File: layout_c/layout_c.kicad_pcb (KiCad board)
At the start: 2 copper layers, 84.9 x 53.1 mm, 74 parts, among them J1 platform UART, J10 Conn_01x08, J11 TSM-113-01-L-DH-A-P-TR, J12 Conn_01x04, J2 USB_C_Sensors, J3 CSI2 Camera, J4 Lidar, J5 MSD-4-A, J6 Power, J7 Radar UART, J8 Conn_01x11, J9 USB_C_Radar, Q1 TSM500P02CX_RFG, SW1 RST, U1 MLX90614ESF-BAA-000-TU, U2 USBLC6-2SC6, U3 BNO085, U4 USBLC6-2SC6, U5 ESP32-P4_MODULE, U9 DRV8434PWP

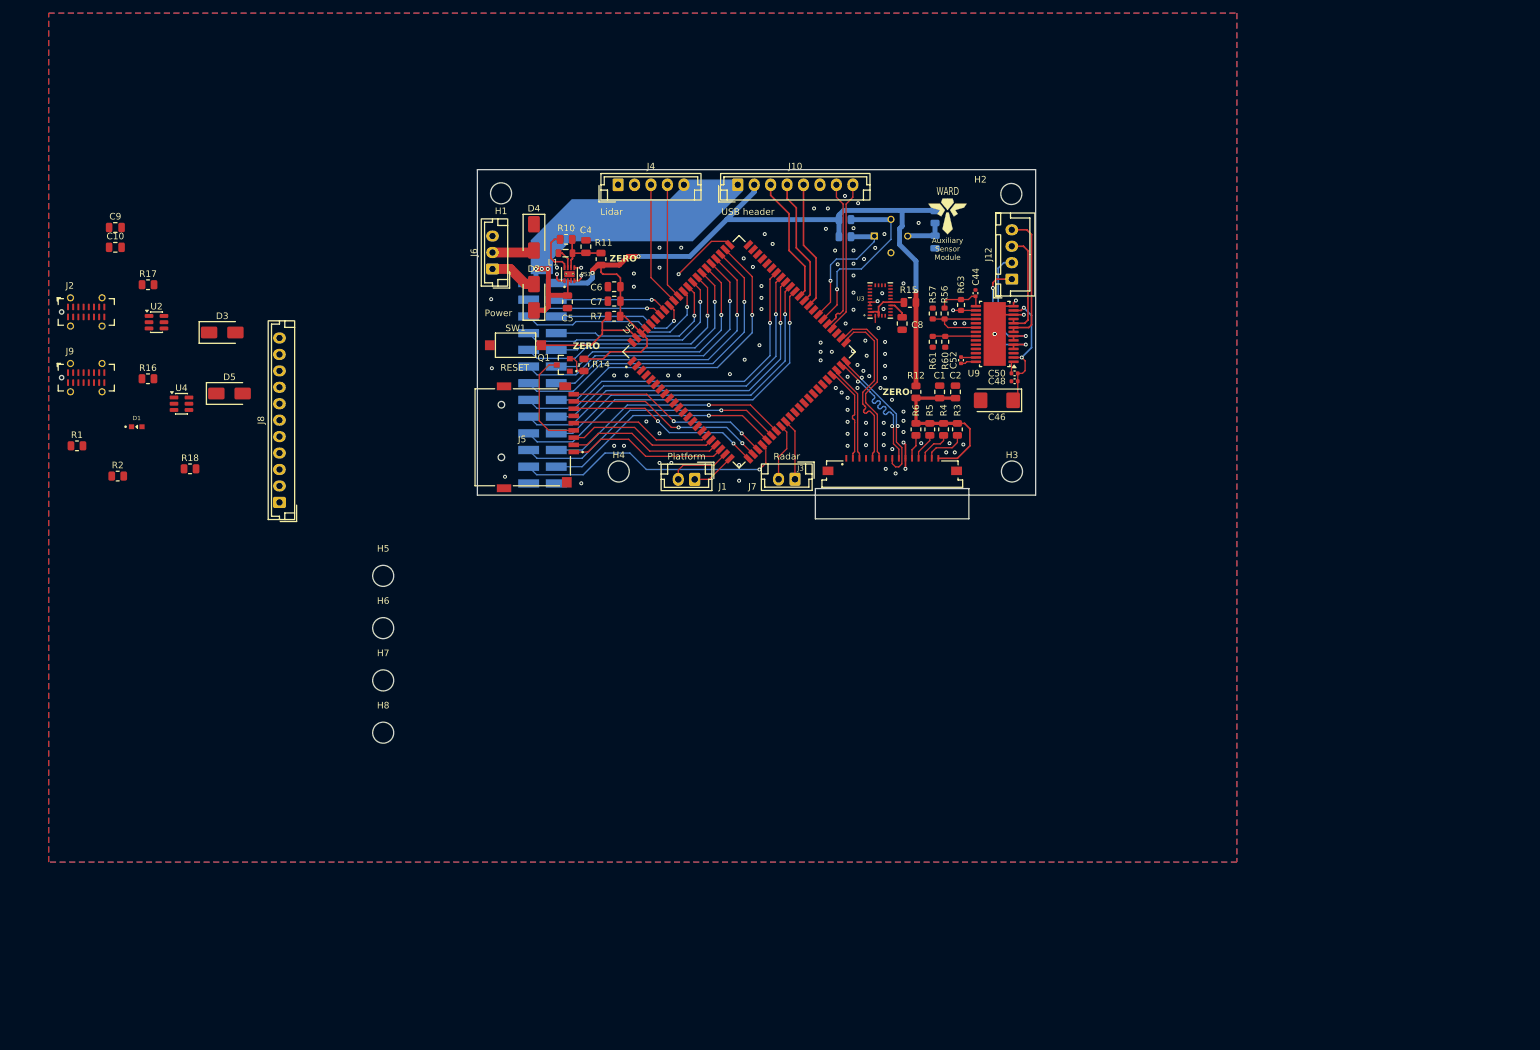
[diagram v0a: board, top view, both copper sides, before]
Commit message: Updated usb footprints on layout C
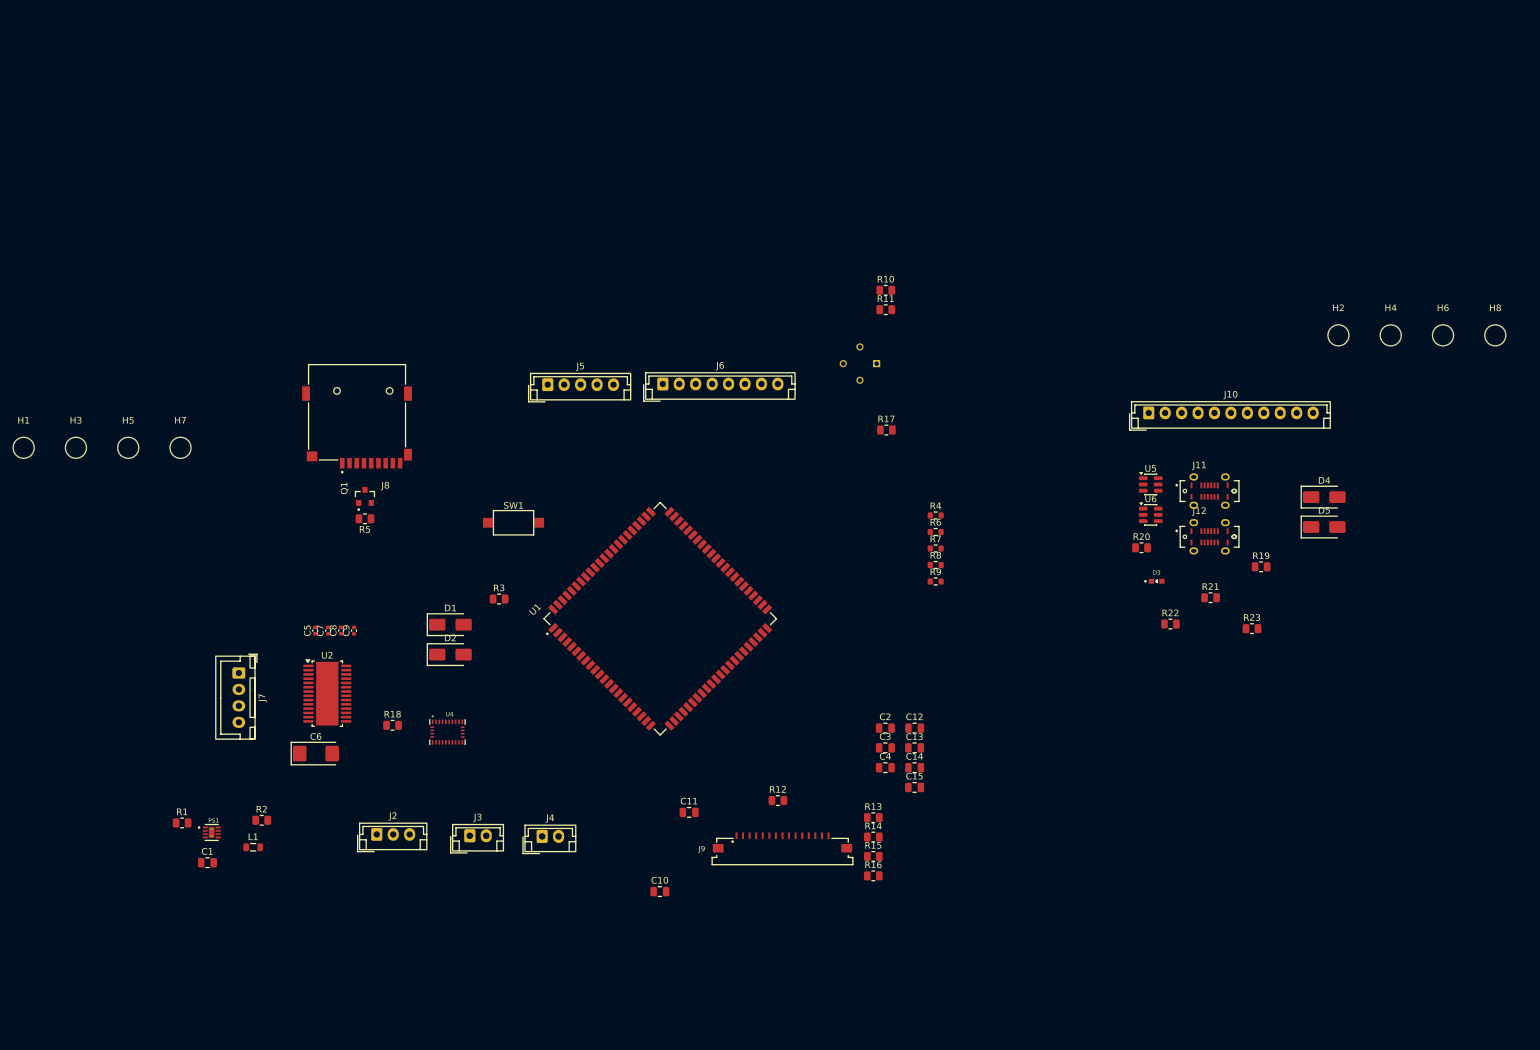
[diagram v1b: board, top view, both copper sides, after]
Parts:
- removed C44: 0.47uF, Capacitor_SMD:C_0402_1005Metric
- removed C46: Bulk, Capacitor_Tantalum_SMD:CP_EIA-6032-15_Kemet-U
- removed C48: 0.1uF, Capacitor_SMD:C_0402_1005Metric
- removed C50: 0.22uF, Capacitor_SMD:C_0402_1005Metric
- removed C52: 0.022uF, Capacitor_SMD:C_0402_1005Metric
- removed CamMnt1: ~, Library:PiCamIndicator
- removed J1: platform UART, Connector_JST:JST_EH_B2B-EH-A_1x02_P2.50mm_Vertical
- removed R56, R57, R60, R61: R, Resistor_SMD:R_0603_1608Metric
- removed R63: 10k, Resistor_SMD:R_0603_1608Metric
- removed U9: DRV8434PWP, Package_SO:TSSOP-28-1EP_4.4x9.7mm_P0.65mm_EP3.4x9.7mm_Mask3.1x4.05mm
- added C11: 100n, Capacitor_SMD:C_0805_2012Metric, F.Cu at (154.9, 149.6)
- added C12: 100n, Capacitor_SMD:C_0805_2012Metric, F.Cu at (189.2, 136.7)
- added C13: 100n, Capacitor_SMD:C_0805_2012Metric, F.Cu at (189.2, 139.7)
- added C14: 10u, Capacitor_SMD:C_0805_2012Metric, F.Cu at (189.2, 142.7)
- added C15: 100n, Capacitor_SMD:C_0805_2012Metric, F.Cu at (189.2, 145.8)
- added R19: 5k1, Resistor_SMD:R_0805_2012Metric, F.Cu at (241.9, 112.2)
- added R20: 5k1, Resistor_SMD:R_0805_2012Metric, F.Cu at (223.7, 109.3)
- added R21: 5k1, Resistor_SMD:R_0805_2012Metric, F.Cu at (234.2, 116.9)
- added R22: 5k1, Resistor_SMD:R_0805_2012Metric, F.Cu at (228.1, 120.9)
- added R23: 5k1, Resistor_SMD:R_0805_2012Metric, F.Cu at (240.5, 121.6)
- added U6: USBLC6-2SC6, Package_TO_SOT_SMD:SOT-23-6, F.Cu at (225.1, 104.3)
- C1, C10: value 100n -> 10u
- C2: value 10u -> 100n
- C3: value 100n -> 10u; moved to F.Cu
- C5: value 10u -> 0.47uF; footprint Capacitor_SMD:C_0805_2012Metric -> Capacitor_SMD:C_0402_1005Metric
- C6: value 10u -> Bulk; footprint Capacitor_SMD:C_0805_2012Metric -> Capacitor_Tantalum_SMD:CP_EIA-6032-15_Kemet-U
- C7: value 100n -> 0.1uF; footprint Capacitor_SMD:C_0805_2012Metric -> Capacitor_SMD:C_0402_1005Metric
- C8: value 100n -> 0.22uF; footprint Capacitor_SMD:C_0805_2012Metric -> Capacitor_SMD:C_0402_1005Metric
- C9: value 10u -> 0.022uF; footprint Capacitor_SMD:C_0805_2012Metric -> Capacitor_SMD:C_0402_1005Metric
- D1: value WL-SMCD_0603 -> SS34; footprint Library:WL-SMCD_0603 -> Diode_SMD:D_SMA
- D3: value SS34 -> WL-SMCD_0603; footprint Diode_SMD:D_SMA -> Library:WL-SMCD_0603
- J10: value Conn_01x08 -> Conn_01x11; footprint Connector_JST:JST_EH_B8B-EH-A_1x08_P2.50mm_Vertical -> Connector_JST:JST_EH_B11B-EH-A_1x11_P2.50mm_Vertical
- J11: value TSM-113-01-L-DH-A-P-TR -> USB4120-03-C_REVA6; footprint Library:SAMTEC_TSM-113-01-L-DH-A-P-TR -> Library:GCT_USB4120-03-C_REVA6; moved to F.Cu
- J12: value Conn_01x04 -> USB4120-03-C_REVA6; footprint Connector_JST:JST_XH_B4B-XH-A_1x04_P2.50mm_Vertical -> Library:GCT_USB4120-03-C_REVA6
- J2: value USB_C_Sensors -> Power; footprint Connector_USB:USB_C_Receptacle_G-Switch_GT-USB-7051x -> Connector_JST:JST_EH_B3B-EH-A_1x03_P2.50mm_Vertical
- J3: value CSI2 Camera -> platform UART; footprint Library:686115183522 -> Connector_JST:JST_EH_B2B-EH-A_1x02_P2.50mm_Vertical
- J4: value Lidar -> Radar UART; footprint Connector_JST:JST_EH_B5B-EH-A_1x05_P2.50mm_Vertical -> Connector_JST:JST_EH_B2B-EH-A_1x02_P2.50mm_Vertical
- J5: value MSD-4-A -> Lidar; footprint Library:CUI_MSD-4-A -> Connector_JST:JST_EH_B5B-EH-A_1x05_P2.50mm_Vertical
- J6: value Power -> Conn_01x08; footprint Connector_JST:JST_EH_B3B-EH-A_1x03_P2.50mm_Vertical -> Connector_JST:JST_EH_B8B-EH-A_1x08_P2.50mm_Vertical
- J7: value Radar UART -> Conn_01x04; footprint Connector_JST:JST_EH_B2B-EH-A_1x02_P2.50mm_Vertical -> Connector_JST:JST_XH_B4B-XH-A_1x04_P2.50mm_Vertical
- J8: value Conn_01x11 -> MSD-4-A; footprint Connector_JST:JST_EH_B11B-EH-A_1x11_P2.50mm_Vertical -> Library:CUI_MSD-4-A
- J9: value USB_C_Radar -> CSI2 Camera; footprint Connector_USB:USB_C_Receptacle_G-Switch_GT-USB-7051x -> Library:686115183522
- R10: value 5k1 -> 3k3
- R11: value 0 -> 3k3
- R13: value 0 -> 10k; moved to F.Cu
- R14: value 0 -> NC
- R15: value 0 -> 2k2
- R16: value 5k1 -> 2k2
- R17, R18, R2: value 5k1 -> 0
- R3: value 2k2 -> 10k
- R4: value 2k2 -> 10k; footprint Resistor_SMD:R_0805_2012Metric -> Resistor_SMD:R_0603_1608Metric
- R5: value NC -> 0
- R6, R7: value 10k -> R; footprint Resistor_SMD:R_0805_2012Metric -> Resistor_SMD:R_0603_1608Metric
- R8, R9: value 3k3 -> R; footprint Resistor_SMD:R_0805_2012Metric -> Resistor_SMD:R_0603_1608Metric; moved to F.Cu
- U1: value MLX90614ESF-BAA-000-TU -> ESP32-P4_MODULE; footprint Library:MLX9061_TO254P942H425-4 -> Library:XCVR_ESP32-P4_MODULE; moved to F.Cu
- U2: value USBLC6-2SC6 -> DRV8434PWP; footprint Package_TO_SOT_SMD:SOT-23-6 -> Package_SO:TSSOP-28-1EP_4.4x9.7mm_P0.65mm_EP3.4x9.7mm_Mask3.1x4.05mm
- U3: value BNO085 -> MLX90614ESF-BAA-000-TU; footprint Library:IC_BNO085 -> Library:MLX9061_TO254P942H425-4; moved to B.Cu
- U4: value USBLC6-2SC6 -> BNO085; footprint Package_TO_SOT_SMD:SOT-23-6 -> Library:IC_BNO085
- U5: value ESP32-P4_MODULE -> USBLC6-2SC6; footprint Library:XCVR_ESP32-P4_MODULE -> Package_TO_SOT_SMD:SOT-23-6
- moved H8 179.6 mm to (277.5, 77.0)
- moved D5 167.7 mm to (251.5, 106.2)
- moved H6 167.2 mm to (269.6, 77.0)
- moved D3 147.1 mm to (226.0, 114.4)
- moved H3 142.4 mm to (61.6, 94.1)
- moved R16 133.7 mm to (182.9, 159.2)
- moved C1 132.4 mm to (81.7, 157.2), turned to 0 degrees
- moved C10 128.3 mm to (150.4, 161.6)
- moved J9 127.8 mm to (169.1, 155.0)
- moved D4 126.5 mm to (251.5, 101.6), turned to 0 degrees
- moved H4 119.2 mm to (261.6, 77.0)
- moved R17 114.4 mm to (184.9, 91.4)
- moved L1 102.1 mm to (88.6, 154.8)
- moved PS1 100.8 mm to (82.3, 152.6), turned to 0 degrees
- moved J4 99.8 mm to (132.6, 153.2)
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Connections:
- C1 pad 1: Net-(C1-Pad1) -> +5V
- C10 pad 1: /IO plate/IO_3V3 -> Net-(C10-Pad1)
- C2 pad 1: Net-(C1-Pad1) -> Net-(PS1-VOS)
- C3 pad 1: Net-(U1-VDD) -> GND
- C3 pad 2: GND -> +3V3
- C4 pad 1: Net-(PS1-VOS) -> GND
- C4 pad 2: GND -> +3V3
- C6 pad 1: GND -> /layout_c/V_m
- C6 pad 2: +3V3 -> GND
- C7 pad 1: GND -> /layout_c/V_m
- C7 pad 2: +3V3 -> GND
- C8 pad 1: GND -> /layout_c/V_m
- C8 pad 2: Net-(U3-CAP) -> Net-(U2-VCP)
- C9 pad 1: /IO plate/IO_3V3 -> Net-(U2-CPH)
- C9 pad 2: GND -> Net-(U2-CPL)
- D1 pad 1: Net-(D1-Pad1) -> +5V
- D1 pad 2: /IO plate/IO_LED -> Net-(D1-A)
- D2 pad 1: +5V -> +12V
- D3 pad 1: /IO plate/IO_5V -> Net-(D3-Pad1)
- D3 pad 2: VBUS1 -> /IO plate/IO_LED
- D4 pad 1: +12V -> /IO plate/IO_5V
- D4 pad 2: Net-(D4-A) -> VBUS2
- J10 pad 1: +5V -> /IO plate/D1-
- J10 pad 2: +3V3 -> /IO plate/D1+
- J10 pad 3: /layout_b/SCL -> GND
- J10 pad 4: /layout_b/SDA -> /IO plate/IO_LED
- J10 pad 5: /layout_b/LED -> /IO plate/IO_SDA
- J10 pad 6: GND -> /IO plate/IO_SCL
- J10 pad 7: /layout_b/usb+ -> /IO plate/IO_3V3
- J10 pad 8: /layout_b/usb- -> /IO plate/IO_5V
- J3 pad 1: GND -> /layout_c/PTX
- J3 pad 2: /layout_b/CSI_D0- -> /layout_c/PRX
- J4 pad 1: unconnected-(J4-Pin_1-Pad1) -> /layout_c/RTX
- J4 pad 2: GND -> /layout_c/RRX
- J5 pad 1: /layout_b/D2 -> unconnected-(J5-Pin_1-Pad1)
- J5 pad 2: /layout_b/D3 -> GND
- J5 pad 3: /layout_b/SDCMD -> /layout_c/LRX
- J5 pad 4: /layout_b/SD_VDD -> /layout_c/LTX
- J5 pad 5: /layout_b/SDCLK -> +5V
- J6 pad 1: Net-(D2-A) -> +5V
- J6 pad 2: Net-(D4-A) -> +3V3
- J6 pad 3: GND -> /layout_c/SCL
- J7 pad 1: /layout_b/RTX -> Net-(J7-Pin_1)
- J7 pad 2: /layout_b/RRX -> Net-(J7-Pin_2)
- J8 pad 1: /IO plate/D1- -> /layout_c/D2
- J8 pad 2: /IO plate/D1+ -> /layout_c/D3
- J8 pad 3: GND -> /layout_c/SDCMD
- J8 pad 4: /IO plate/IO_LED -> /layout_c/SD_VDD
- J8 pad 5: /IO plate/IO_SDA -> /layout_c/SDCLK
- J8 pad 6: /IO plate/IO_SCL -> GND
- J8 pad 7: /IO plate/IO_3V3 -> /layout_c/D0
- J8 pad 8: /IO plate/IO_5V -> /layout_c/D1
- Q1 pad 3: /layout_b/SD_VDD -> /layout_c/SD_VDD
- R1 pad 1: Net-(J2-CC1) -> Net-(PS1-PG)
- R1 pad 2: GND -> Net-(PS1-VOS)
- R10 pad 1: Net-(PS1-PG) -> /layout_c/TEMP_SCL
- R10 pad 2: Net-(PS1-VOS) -> +3V3
- R11 pad 1: +3V3 -> /layout_c/TEMP_SDA
- R11 pad 2: Net-(PS1-VOS) -> +3V3
- R12 pad 2: Net-(C1-Pad1) -> Net-(C10-Pad1)
- R13 pad 1: +3V3 -> Net-(C10-Pad1)
- R13 pad 2: Net-(U1-VDD) -> /layout_c/CSI0
- R14 pad 1: +3V3 -> Net-(C10-Pad1)
- R14 pad 2: Net-(Q1-Pad2) -> /layout_c/CSI1
- R15 pad 1: +3V3 -> Net-(C10-Pad1)
- R15 pad 2: /layout_b/IMU_VDD -> /layout_c/I2C SCL
- R16 pad 1: Net-(J9-CC1) -> Net-(C10-Pad1)
- R16 pad 2: GND -> /layout_c/I2C SDA
- R17 pad 1: Net-(J9-CC2) -> +3V3
- R17 pad 2: GND -> Net-(U3-VDD)
- R18 pad 1: GND -> +3V3
- R18 pad 2: Net-(D1-Pad1) -> /layout_c/IMU_VDD
- R2 pad 1: Net-(J2-CC2) -> +3V3
- R2 pad 2: GND -> Net-(PS1-VOS)
- R3 pad 1: Net-(C1-Pad1) -> Net-(U1-ESP_EN)
- R3 pad 2: /layout_b/I2C SDA -> +3V3
- R4 pad 1: Net-(C1-Pad1) -> Net-(U2-~{FAULT})
- R4 pad 2: /layout_b/I2C SCL -> +5V
- R5 pad 1: Net-(C1-Pad1) -> +3V3
- R5 pad 2: /layout_b/CSI1 -> Net-(Q1-Pad2)
- R6 pad 1: Net-(C1-Pad1) -> /layout_c/M0
- R6 pad 2: /layout_b/CSI0 -> +5V
- R7 pad 1: Net-(U5-ESP_EN) -> /layout_c/M0
- R7 pad 2: +3V3 -> GND
- R8 pad 1: /layout_b/TEMP_SDA -> /layout_c/M1
- R8 pad 2: +3V3 -> +5V
- R9 pad 1: /layout_b/TEMP_SCL -> /layout_c/M1
- R9 pad 2: +3V3 -> GND
- SW1 pad 2: Net-(U5-ESP_EN) -> Net-(U1-ESP_EN)
- U1 pad 1: /layout_b/TEMP_SCL -> GND
- U1 pad 2: /layout_b/TEMP_SDA -> unconnected-(U1-LNA_OUT-Pad2)
- U1 pad 3: Net-(U1-VDD) -> GND
- U1 pad 4: GND -> unconnected-(U1-C6_U0RXD-Pad4)
- U2 pad 1: /IO plate/d1- -> Net-(U2-VCP)
- U2 pad 2: GND -> /layout_c/V_m
- U2 pad 3: /IO plate/d1+ -> GND
- U2 pad 4: /IO plate/D1+ -> Net-(J7-Pin_1)
- U2 pad 5: VBUS1 -> Net-(J7-Pin_1)
- U2 pad 6: /IO plate/D1- -> Net-(J7-Pin_2)
- U3 pad 1: unconnected-(U3-RESV_NC-Pad1) -> /layout_c/TEMP_SCL
- U3 pad 2: GND -> /layout_c/TEMP_SDA
- U3 pad 3: /layout_b/IMU_VDD -> Net-(U3-VDD)
- U3 pad 4: unconnected-(U3-~{BOOT}-Pad4) -> GND
- U4 pad 1: /IO plate/d2- -> unconnected-(U4-RESV_NC-Pad1)
- U4 pad 3: /IO plate/d2+ -> /layout_c/IMU_VDD
- U4 pad 4: /IO plate/D2+ -> unconnected-(U4-~{BOOT}-Pad4)
- U4 pad 5: VBUS2 -> unconnected-(U4-PS1-Pad5)
- U4 pad 6: /IO plate/D2- -> unconnected-(U4-PS0/WAKE-Pad6)
- U5 pad 1: GND -> /IO plate/d1-
- U5 pad 2: unconnected-(U5-LNA_OUT-Pad2) -> GND
- U5 pad 3: GND -> /IO plate/d1+
- U5 pad 4: unconnected-(U5-C6_U0RXD-Pad4) -> /IO plate/D1+
- U5 pad 5: unconnected-(U5-C6_U0TXD-Pad5) -> VBUS2
- U5 pad 6: unconnected-(U5-C6_IO15-Pad6) -> /IO plate/D1-
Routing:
- net +3V3: track 128.9 -> 0.00 mm, vias 3 -> 0
- net /layout_b/29: track 56.4 -> 0.00 mm, vias 1 -> 0
- net /layout_b/31: track 55.0 -> 0.00 mm, vias 1 -> 0
- net /layout_b/33: track 53.6 -> 0.00 mm, vias 1 -> 0
- net /layout_b/30: track 51.0 -> 0.00 mm, vias 1 -> 0
- net /layout_b/41: track 50.4 -> 0.00 mm, vias 1 -> 0
- net /layout_b/32: track 49.5 -> 0.00 mm, vias 1 -> 0
- net /layout_b/40: track 48.4 -> 0.00 mm, vias 1 -> 0
- net /layout_b/43: track 45.2 -> 0.00 mm, vias 1 -> 0
- net /layout_b/42: track 43.1 -> 0.00 mm, vias 1 -> 0
- net /layout_b/11: track 42.4 -> 0.00 mm, vias 1 -> 0
- net /layout_b/13: track 42.1 -> 0.00 mm, vias 1 -> 0
- net /layout_b/45: track 40.0 -> 0.00 mm, vias 1 -> 0
- net /layout_b/20: track 37.9 -> 0.00 mm, vias 1 -> 0
- net /layout_b/44: track 37.8 -> 0.00 mm, vias 1 -> 0
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- removed copper zone on B.Cu, net GND
- removed copper zone on F.Cu, net GND
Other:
- board size 84.9 x 53.1 mm -> 0.7 x 0.5 mm
- board text removed: "+5V"
- board text removed: "Auxiliary Sensor Module"
- board text removed: "Lidar"
- board text removed: "Platform"
- board text removed: "Power"
- board text removed: "RESET"
- board text removed: "Radar"
- board text removed: "USB header"
- board text removed: "WARD"
- board text removed: "ZERO"

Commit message: Layout C adjusted
switched to 4 layer stack
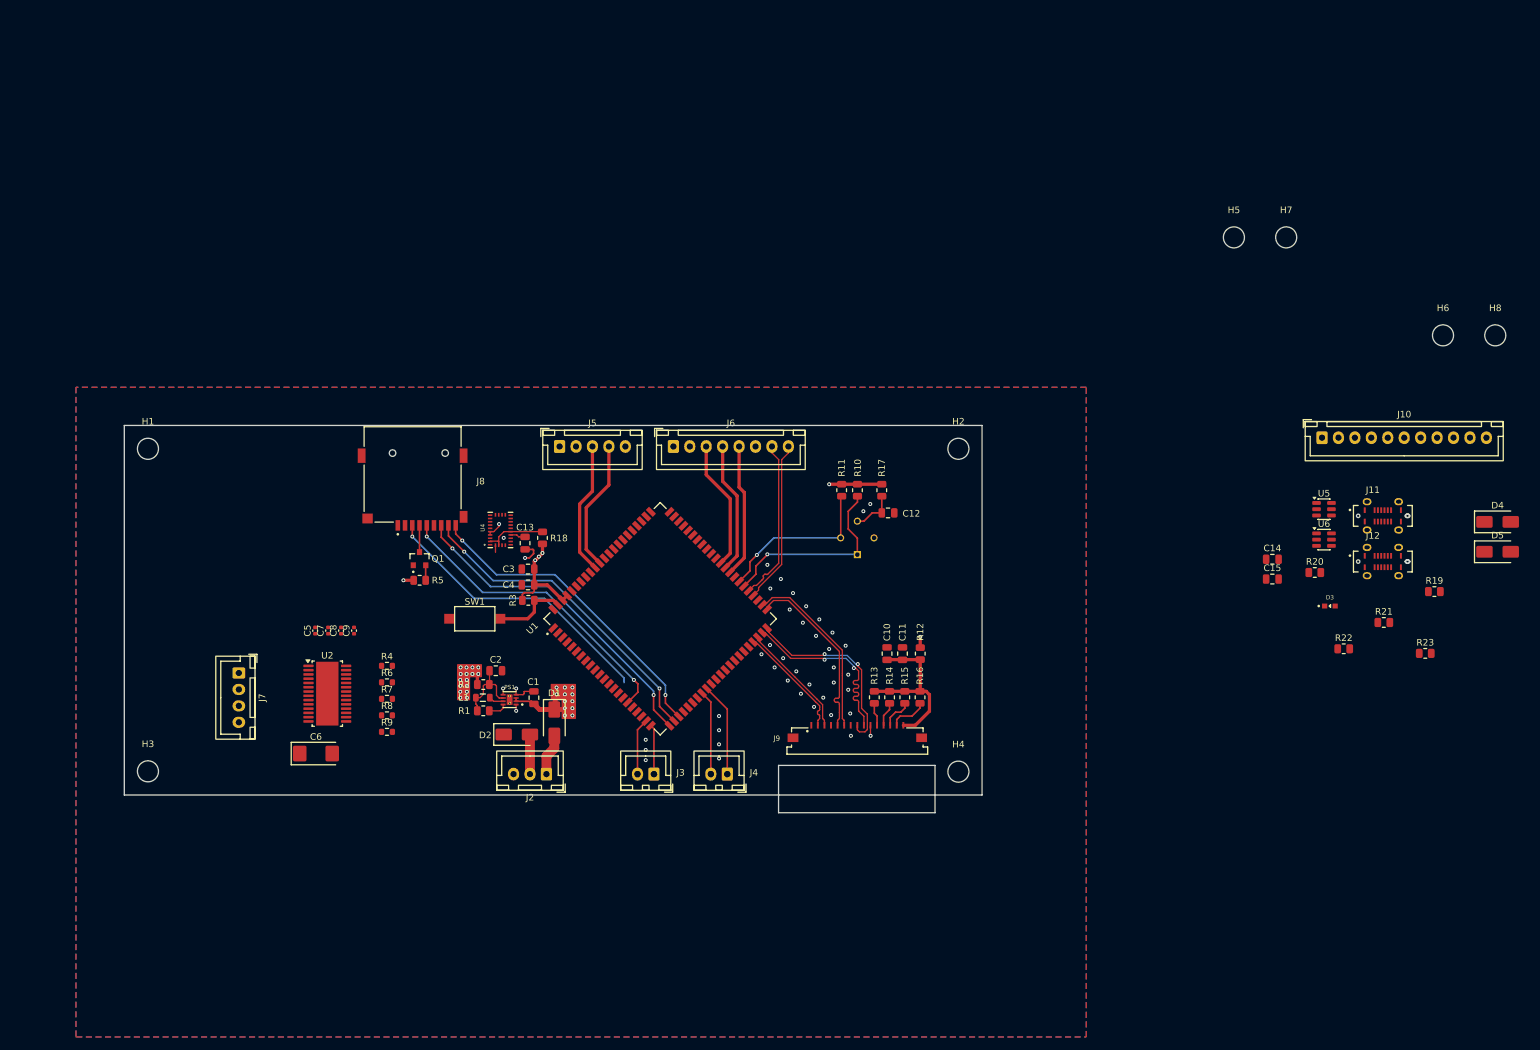
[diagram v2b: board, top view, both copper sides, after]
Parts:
- J10: footprint Connector_JST:JST_EH_B11B-EH-A_1x11_P2.50mm_Vertical -> Connector_JST:JST_XH_B11B-XH-A_1x11_P2.50mm_Vertical
- J2: footprint Connector_JST:JST_EH_B3B-EH-A_1x03_P2.50mm_Vertical -> Connector_JST:JST_XH_B3B-XH-A_1x03_P2.50mm_Vertical
- J3, J4: footprint Connector_JST:JST_EH_B2B-EH-A_1x02_P2.50mm_Vertical -> Connector_JST:JST_XH_B2B-XH-A_1x02_P2.50mm_Vertical
- J5: footprint Connector_JST:JST_EH_B5B-EH-A_1x05_P2.50mm_Vertical -> Connector_JST:JST_XH_B5B-XH-A_1x05_P2.50mm_Vertical
- J6: footprint Connector_JST:JST_EH_B8B-EH-A_1x08_P2.50mm_Vertical -> Connector_JST:JST_XH_B8B-XH-A_1x08_P2.50mm_Vertical
- moved H5 171.2 mm to (237.8, 62.1)
- moved H7 171.2 mm to (245.7, 62.1)
- moved H4 93.4 mm to (195.8, 143.3)
- moved R4 86.5 mm to (109.0, 127.3)
- moved R6 86.5 mm to (109.0, 129.8)
- moved R7 86.5 mm to (109.0, 132.3)
- moved R8 86.5 mm to (109.0, 134.8)
- moved R9 86.5 mm to (109.0, 137.3)
- moved C13 66.9 mm to (129.9, 108.6), turned to 90 degrees
- moved C14 63.0 mm to (243.6, 111.0)
- moved C15 63.0 mm to (243.6, 114.1)
- moved C4 61.0 mm to (130.4, 115.0)
- moved C3 60.8 mm to (130.4, 112.5)
- moved H2 60.3 mm to (195.8, 94.2)
- moved C2 59.9 mm to (125.5, 128.0)
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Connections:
- U1 pad 50: /layout_c/TEMP_SDA -> /layout_c/TEMP_SCL
- U1 pad 51: /layout_c/TEMP_SCL -> /layout_c/TEMP_SDA
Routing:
- net +5V: track 0.00 -> 61.9 mm, vias 0 -> 12
- net /layout_c/D0: track 0.00 -> 50.1 mm, vias 0 -> 2
- net /layout_c/D1: track 0.00 -> 49.2 mm, vias 0 -> 2
- net /layout_c/CD: track 0.00 -> 48.3 mm, vias 0 -> 2
- net /layout_c/SDCLK: track 0.00 -> 46.5 mm, vias 0 -> 2
- net /layout_c/SDCMD: track 0.00 -> 43.5 mm, vias 0 -> 1
- net /layout_c/TEMP_SCL: track 0.00 -> 30.4 mm, vias 0 -> 1
- net /layout_c/CSI_CLK-: track 0.00 -> 29.5 mm, vias 0 -> 2
- net /layout_c/CSI_CLK+: track 0.00 -> 29.4 mm, vias 0 -> 2
- net +3V3: track 0.00 -> 29.1 mm, vias 0 -> 22
- net /layout_c/CSI_D1+: track 0.00 -> 27.5 mm
- net /layout_c/CSI_D1-: track 0.00 -> 27.4 mm
- net Net-(C10-Pad1): track 0.00 -> 25.9 mm
- net /layout_c/TEMP_SDA: track 0.00 -> 25.4 mm, vias 0 -> 1
- net /layout_c/usb-: track 0.00 -> 24.9 mm
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- added copper zone on In1.Cu, net +3V3
- added copper zone on B.Cu, net GND
- added copper zone on F.Cu, net GND
- added copper zone on In2.Cu, net GND
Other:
- board size 0.7 x 0.5 mm -> 130.4 x 58.9 mm
- copper layers 2 -> 4

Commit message: Updated layout C
implemented stepper driver
tighter layout
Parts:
- added R24: 0, Resistor_SMD:R_0805_2012Metric, F.Cu at (103.4, 119.3)
- J4: footprint Connector_JST:JST_XH_B2B-XH-A_1x02_P2.50mm_Vertical -> Connector_JST:JST_XH_B5B-XH-A_1x05_P2.50mm_Vertical
- moved J7 36.9 mm to (101.5, 94.7)
- moved H1 32.8 mm to (101.1, 78.0)
- moved H3 32.8 mm to (101.1, 127.1)
- moved C6 32.2 mm to (105.4, 109.2), turned to 90 degrees
- moved U2 23.6 mm to (113.5, 112.2), turned to -90 degrees
- moved C8 21.6 mm to (117.6, 107.0), turned to 0 degrees
- moved R9 18.6 mm to (113.6, 119.3), turned to -90 degrees
- moved C7 18.3 mm to (109.9, 106.5)
- moved J4 16.6 mm to (164.1, 127.5)
- moved J3 16.5 mm to (146.2, 127.5)
- moved R13 16.2 mm to (184.3, 115.8)
- moved R14 16.2 mm to (186.6, 115.8)
- moved R15 16.2 mm to (188.9, 115.8)
- moved R16 16.2 mm to (191.2, 115.8)
- moved J11 16.2 mm to (261.6, 88.2)
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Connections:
- Q1 pad 1: unconnected-(Q1-Pad1) -> /layout_c/SDEN
- U1 pad 16: unconnected-(U1-GPIO1-Pad16) -> /layout_c/SDEN
- U1 pad 17: /layout_c/SDCLK -> /layout_c/SDCMD
- U1 pad 18: /layout_c/SDCMD -> /layout_c/SDCLK
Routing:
- net +5V: track 61.9 -> 134.1 mm, vias 12 -> 16
- net /layout_c/D2: track 0.00 -> 55.4 mm, vias 0 -> 2
- net /layout_c/D3: track 0.00 -> 55.3 mm, vias 0 -> 2
- net /layout_c/SDEN: track 0.00 -> 44.5 mm
- net /layout_c/V_m: track 0.00 -> 27.7 mm, vias 0 -> 2
- net Net-(J7-Pin_1): track 0.00 -> 23.9 mm
- net +12V: track 0.00 -> 23.1 mm, vias 0 -> 22
- net Net-(J7-Pin_2): track 0.00 -> 21.9 mm
- net GND: track 14.7 -> 34.9 mm, vias 45 -> 53
- net Net-(J7-Pin_3): track 0.00 -> 18.5 mm
- net Net-(J7-Pin_4): track 0.00 -> 17.2 mm, vias 0 -> 1
- net /layout_c/M0: track 0.00 -> 9.66 mm
- net /layout_c/SDCLK: track 46.5 -> 55.2 mm
- net Net-(U2-~{FAULT}): track 0.00 -> 6.32 mm
- net /layout_c/D1: track 49.2 -> 55.3 mm
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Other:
- board size 130.4 x 58.9 mm -> 103.4 x 58.9 mm
- board text added: "Auxiliary Sensor Module"
- board text added: "Lidar"
- board text added: "POWER"
- board text added: "Platform UART"
- board text added: "Radar Unit"
- board text added: "Stepper"
- board text added: "Stepper config"
- board text added: "USB Interface"
- board text added: "WARD"
